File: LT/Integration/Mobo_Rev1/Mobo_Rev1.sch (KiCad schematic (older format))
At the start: 0 parts

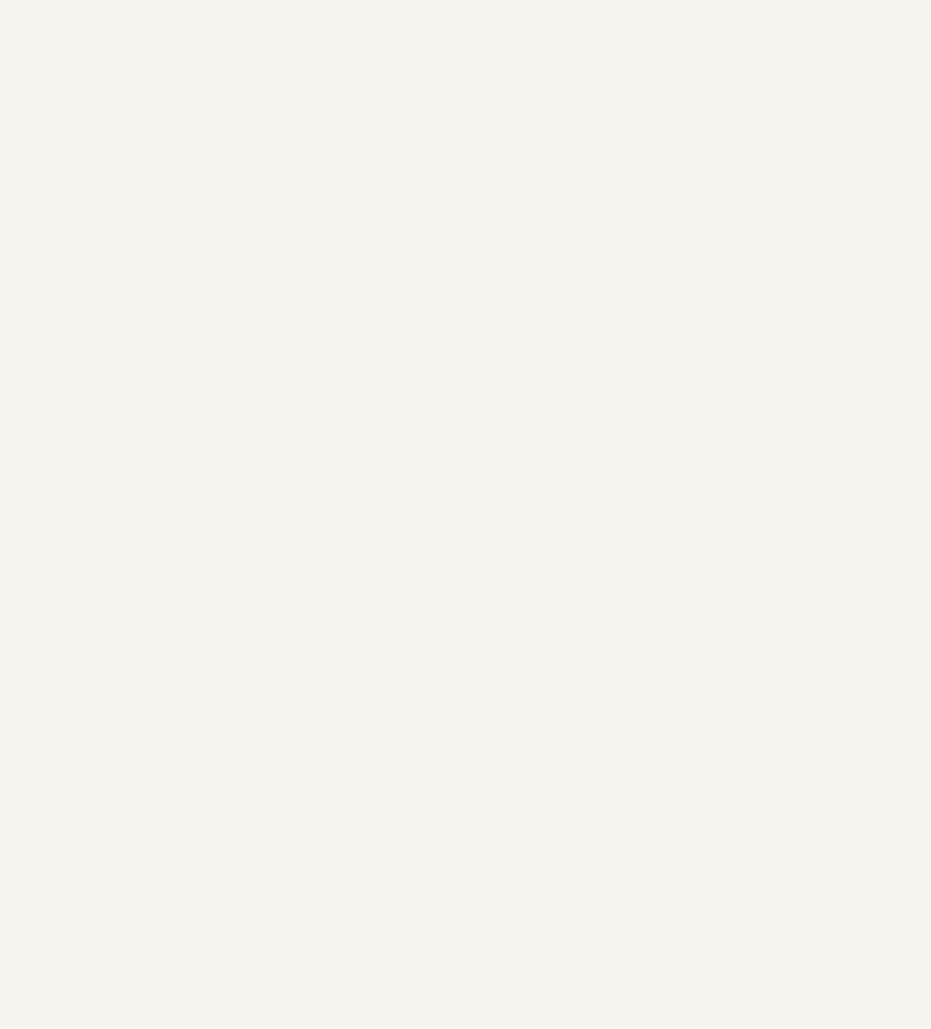
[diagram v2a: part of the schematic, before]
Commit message: imported Mobo standard board
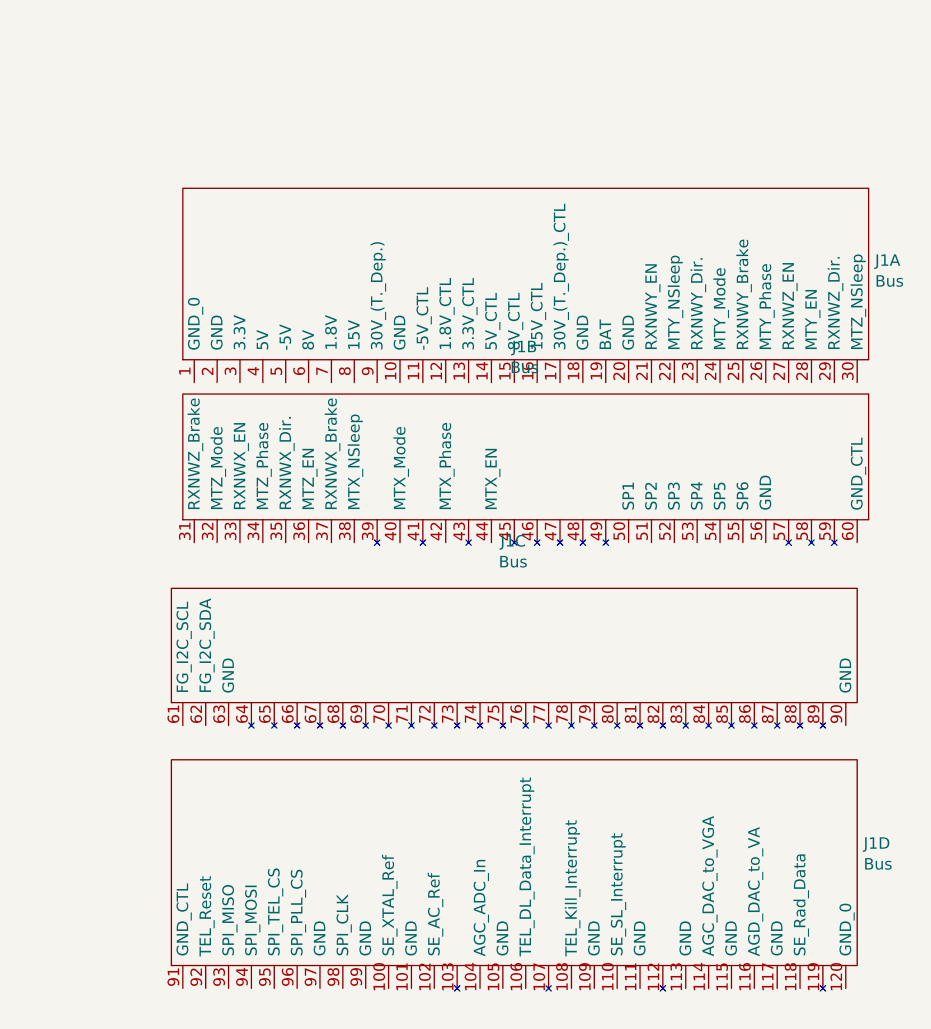
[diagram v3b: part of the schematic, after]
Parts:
- added J1: Bus, SS:STD_PCB_A1_v1.1, symbol SS:Bus
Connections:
- new net: J1.104, J1.~ (AGC_ADC_In)
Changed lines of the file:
@@
 Text Notes 3600 4800 0    118  ~ 0
 Notch Filters
+$Comp
+L SS:Bus J1
+U 1 1 5E4D68DD
+P 8800 2900
+F 0 "J1" H 10328 3434 50  0000 L CNN
+F 1 "Bus" H 10328 3343 50  0000 L CNN
+F 2 "SS:STD_PCB_A1_v1.1" H 7500 3950 50  0001 C CNN
+F 3 "" H 7500 3950 50  0001 C CNN
+	1    8800 2900
+	1    0    0    -1
+$EndComp
+$Comp
+L SS:Bus J1
+U 2 1 5E4D9735
+P 8800 3600
+F 0 "J1" H 8795 4456 50  0000 C CNN
+F 1 "Bus" H 8795 4365 50  0000 C CNN
+F 2 "SS:STD_PCB_A1_v1.1" H 7500 4650 50  0001 C CNN
+F 3 "" H 7500 4650 50  0001 C CNN
+	2    8800 3600
+	1    0    0    -1
+$EndComp
+$Comp
+L SS:Bus J1
+U 3 1 5E4E007E
+P 8750 4400
+F 0 "J1" H 8745 5206 50  0000 C CNN
+F 1 "Bus" H 8745 5115 50  0000 C CNN
+F 2 "SS:STD_PCB_A1_v1.1" H 7450 5450 50  0001 C CNN
+F 3 "" H 7450 5450 50  0001 C CNN
+	3    8750 4400
+	1    0    0    -1
+$EndComp
+$Comp
+L SS:Bus J1
+U 4 1 5E4E41F8
+P 8750 5550
+F 0 "J1" H 10278 6184 50  0000 L CNN
+F 1 "Bus" H 10278 6093 50  0000 L CNN
+F 2 "SS:STD_PCB_A1_v1.1" H 7450 6600 50  0001 C CNN
+F 3 "" H 7450 6600 50  0001 C CNN
+	4    8750 5550
+	1    0    0    -1
+$EndComp
 $EndSCHEMATC

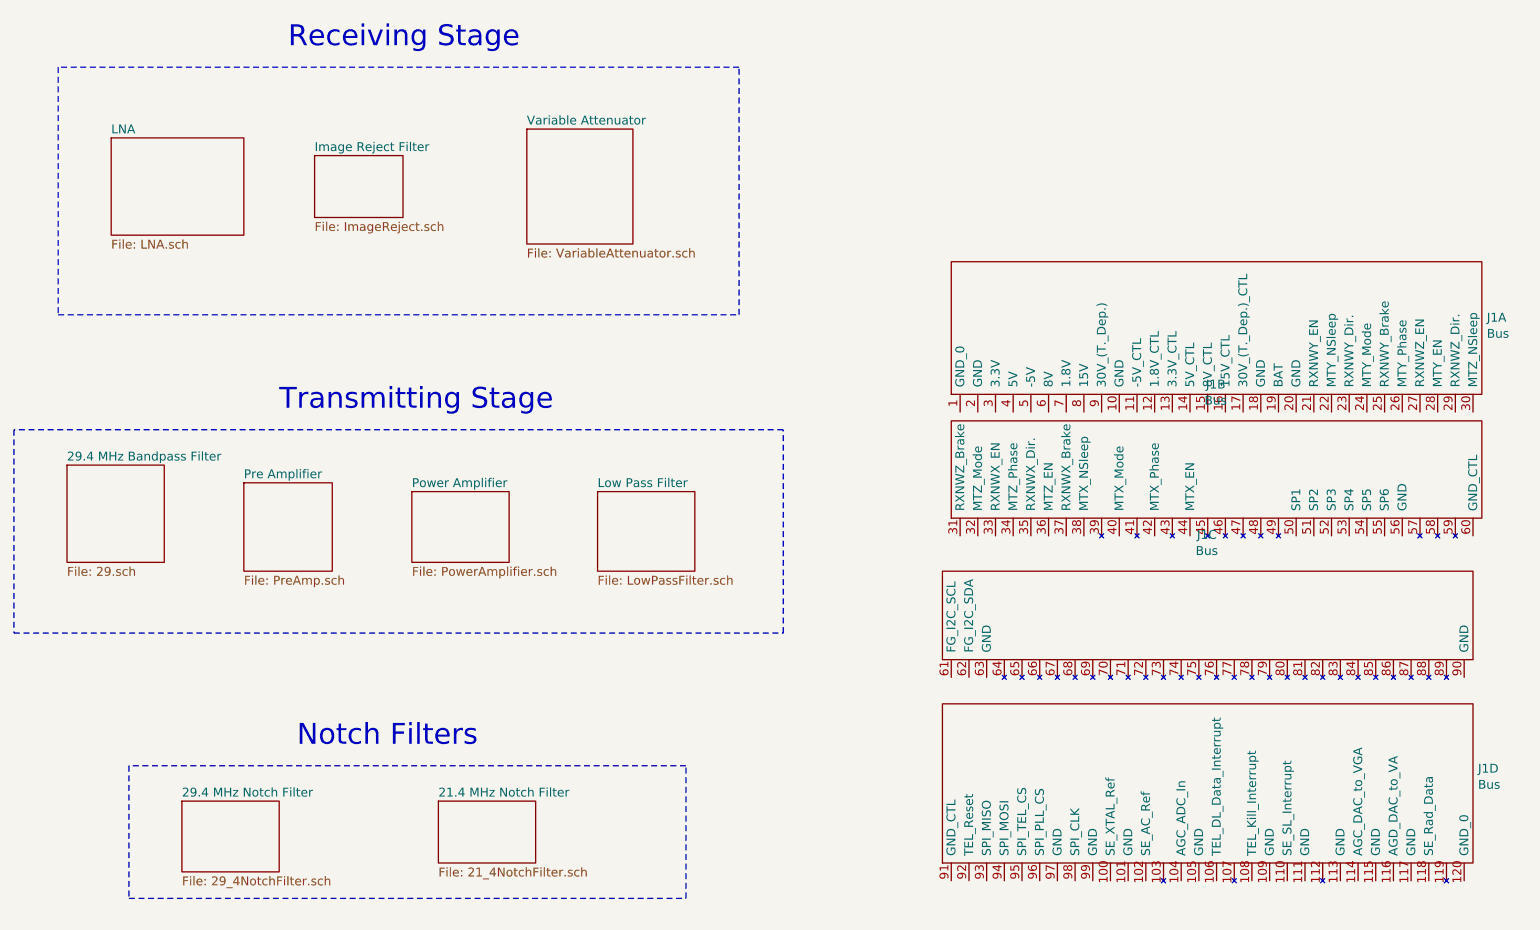
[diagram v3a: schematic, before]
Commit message: MoBo Pretty
Made some changes to the MoBo which included changing the outline boarders for the sheets
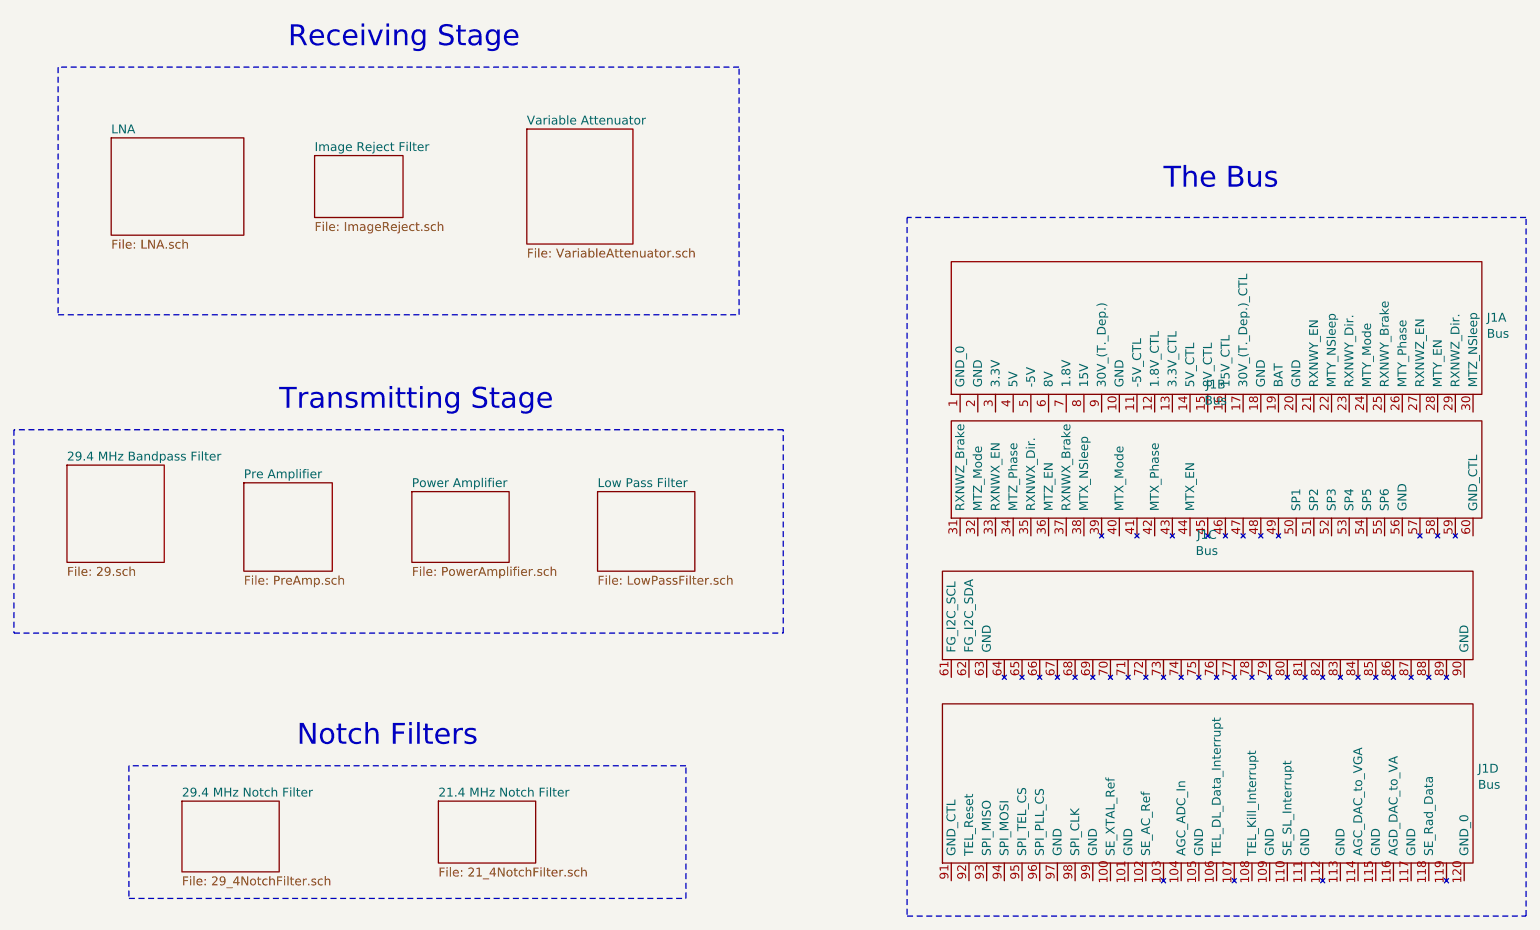
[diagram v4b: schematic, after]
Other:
- note added: "The Bus"
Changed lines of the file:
@@
 Text Notes 3550 850  0    118  ~ 0
 Receiving Stage
-Wire Notes Line width 39 style solid rgb(127, 36, 0)
+Wire Notes Line width 39 style solid rgb(127, 0, 111)
 	2000 3000 2000 4150
-Wire Notes Line width 39 style solid rgb(127, 36, 0)
+Wire Notes Line width 39 style solid rgb(127, 0, 111)
 	2000 4150 6350 4150
-Wire Notes Line width 39 style solid rgb(127, 36, 0)
+Wire Notes Line width 39 style solid rgb(127, 0, 111)
 	6350 4150 6350 3000
-Wire Notes Line width 39 style solid rgb(126, 35, 0)
+Wire Notes Line width 39 style solid rgb(127, 35, 111)
 	6350 3000 2000 3000
 Text Notes 3500 2900 0    118  ~ 0
 Transmitting Stage
-Wire Notes Line width 39 style solid rgb(194, 107, 0)
+Wire Notes Line width 39 style solid rgb(194, 132, 143)
 	2650 4900 2650 5650
-Wire Notes Line width 39 style solid rgb(194, 106, 0)
+Wire Notes Line width 39 style solid rgb(194, 132, 143)
 	2650 5650 5800 5650
-Wire Notes Line width 39 style solid rgb(194, 107, 0)
+Wire Notes Line width 39 style solid rgb(194, 132, 143)
 	5800 5650 5800 4900
-Wire Notes Line width 39 style solid rgb(194, 107, 0)
+Wire Notes Line width 39 style solid rgb(194, 132, 143)
 	5800 4900 2650 4900
 Text Notes 3600 4800 0    118  ~ 0
@@
 	1    0    0    -1
 $EndComp
+Wire Notes Line width 39
+	7050 1800 7050 5750
+Wire Notes Line width 39
+	7050 5750 10550 5750
+Wire Notes Line width 39
+	10550 5750 10550 1800
+Wire Notes Line width 39
+	10550 1800 7050 1800
+Text Notes 8500 1650 0    118  ~ 0
+The Bus
 $EndSCHEMATC

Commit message: Just Testing GitBash, changed a resistor value in LNA
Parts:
- J1: symbol SS:Bus -> Mobo_Rev1-rescue:Bus-SS
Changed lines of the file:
@@
 Notch Filters
 $Comp
-L SS:Bus J1
+L Mobo_Rev1-rescue:Bus-SS J1
 U 1 1 5E4D68DD
 P 8800 2900
@@
 $EndComp
 $Comp
-L SS:Bus J1
+L Mobo_Rev1-rescue:Bus-SS J1
 U 2 1 5E4D9735
 P 8800 3600
@@
 $EndComp
 $Comp
-L SS:Bus J1
+L Mobo_Rev1-rescue:Bus-SS J1
 U 3 1 5E4E007E
 P 8750 4400
@@
 $EndComp
 $Comp
-L SS:Bus J1
+L Mobo_Rev1-rescue:Bus-SS J1
 U 4 1 5E4E41F8
 P 8750 5550
